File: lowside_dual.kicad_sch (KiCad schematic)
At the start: 9 parts, among them U2 2k7, U34 2k7, U35 RED, U37 RED, U38 MBR2H200SFT, U59 MBR2H200SFT, U60 NCV8403ASTT, U61 NCV8403ASTT

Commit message: update
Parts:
- renumbered U2 to R46, U34 to R47
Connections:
- net +12V renamed 12V_LED

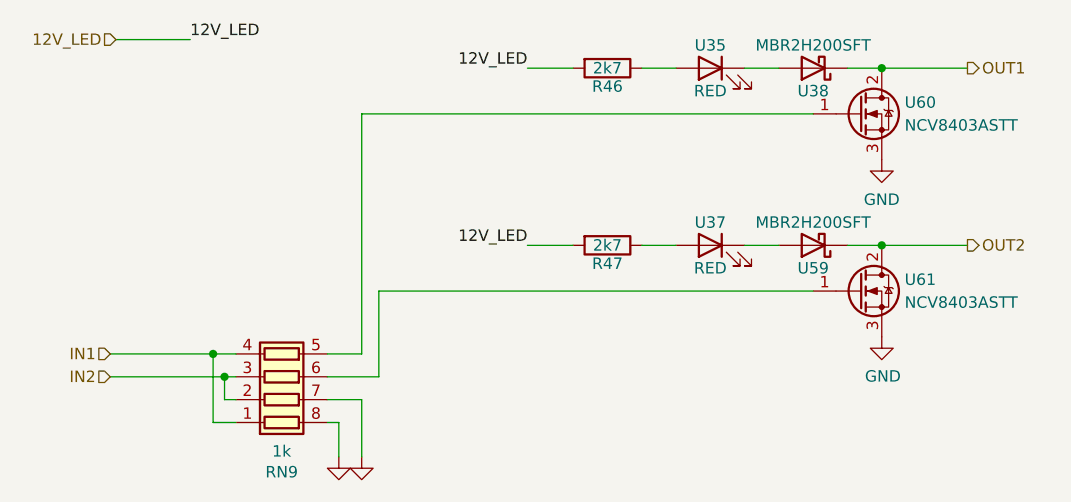
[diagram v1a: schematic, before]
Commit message: USB jack, parts and LCSC numbers, headphone jack
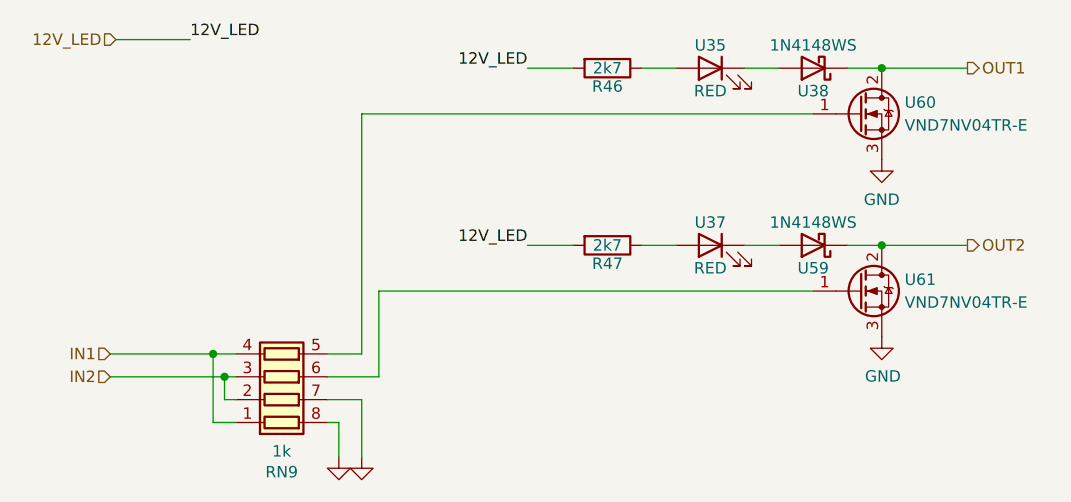
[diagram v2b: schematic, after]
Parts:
- R46, R47: footprint Resistor_SMD:R_0805_2012Metric -> Resistor_SMD:R_0402_1005Metric; LCSC (none) -> C138017
- U35, U37: footprint LED_SMD:LED_0805_2012Metric -> LED_SMD:LED_0603_1608Metric; LCSC (none) -> C84263
- U38, U59: value MBR2H200SFT -> 1N4148WS; footprint Diode_SMD:D_SOD-123 -> Diode_SMD:D_SOD-323; LCSC (none) -> C60580
- U60, U61: value NCV8403ASTT -> VND7NV04TR-E; LCSC (none) -> C155605
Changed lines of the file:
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@@
       (effects (font (size 1.27 1.27)))
     )
-    (property "Footprint" "LED_SMD:LED_0805_2012Metric" (at 161.29 62.865 0)
+    (property "Footprint" "LED_SMD:LED_0603_1608Metric" (at 161.29 62.865 0)
       (effects (font (size 1.27 1.27)) hide)
     )
@@
       (effects (font (size 1.27 1.27)))
     )
+    (property "LCSC" "C84263" (at 161.29 62.865 0)
+      (effects (font (size 1.27 1.27)) hide)
+    )
     (pin "1")
     (pin "2")
@@
       (effects (font (size 1.27 1.27)))
     )
-    (property "Footprint" "Resistor_SMD:R_0805_2012Metric" (at 149.86 61.087 90)
+    (property "Footprint" "Resistor_SMD:R_0402_1005Metric" (at 149.86 61.087 90)
       (effects (font (size 1.27 1.27)) hide)
     )
     (property "Datasheet" "" (at 149.86 62.865 0)
       (effects (font (size 1.27 1.27)))
+    )
+    (property "LCSC" "C138017" (at 149.86 62.865 90)
+      (effects (font (size 1.27 1.27)) hide)
     )
     (pin "1")
@@
       (effects (font (size 1.27 1.27)) (justify left))
     )
-    (property "Value" "NCV8403ASTT" (at 182.88 88.9 0)
+    (property "Value" "VND7NV04TR-E" (at 182.88 88.9 0)
       (effects (font (size 1.27 1.27)) (justify left))
     )
@@
       (effects (font (size 1.27 1.27)) hide)
     )
+    (property "LCSC" "C155605" (at 177.8 87.63 0)
+      (effects (font (size 1.27 1.27)) hide)
+    )
     (pin "1")
     (pin "2")
@@
       (effects (font (size 1.27 1.27)))
     )
-    (property "Footprint" "LED_SMD:LED_0805_2012Metric" (at 161.29 82.55 0)
+    (property "Footprint" "LED_SMD:LED_0603_1608Metric" (at 161.29 82.55 0)
       (effects (font (size 1.27 1.27)) hide)
     )
@@
       (effects (font (size 1.27 1.27)))
     )
+    (property "LCSC" "C84263" (at 161.29 82.55 0)
+      (effects (font (size 1.27 1.27)) hide)
+    )
     (pin "1")
     (pin "2")
@@
       (effects (font (size 1.27 1.27)))
     )
-    (property "Value" "MBR2H200SFT" (at 172.72 60.325 0)
-      (effects (font (size 1.27 1.27)))
-    )
-    (property "Footprint" "Diode_SMD:D_SOD-123" (at 172.72 62.865 0)
+    (property "Value" "1N4148WS" (at 172.72 60.325 0)
+      (effects (font (size 1.27 1.27)))
+    )
+    (property "Footprint" "Diode_SMD:D_SOD-323" (at 172.72 62.865 0)
       (effects (font (size 1.27 1.27)) hide)
     )
@@
       (effects (font (size 1.27 1.27)))
     )
+    (property "LCSC" "C60580" (at 172.72 62.865 0)
+      (effects (font (size 1.27 1.27)) hide)
+    )
     (pin "1")
     (pin "2")
@@
       (effects (font (size 1.27 1.27)))
     )
-    (property "Value" "MBR2H200SFT" (at 172.72 80.01 0)
-      (effects (font (size 1.27 1.27)))
-    )
-    (property "Footprint" "Diode_SMD:D_SOD-123" (at 172.72 82.55 0)
+    (property "Value" "1N4148WS" (at 172.72 80.01 0)
+      (effects (font (size 1.27 1.27)))
+    )
+    (property "Footprint" "Diode_SMD:D_SOD-323" (at 172.72 82.55 0)
       (effects (font (size 1.27 1.27)) hide)
     )
@@
       (effects (font (size 1.27 1.27)))
     )
+    (property "LCSC" "C60580" (at 172.72 82.55 0)
+      (effects (font (size 1.27 1.27)) hide)
+    )
     (pin "1")
     (pin "2")
@@
       (effects (font (size 1.27 1.27)))
     )
-    (property "Footprint" "Resistor_SMD:R_0805_2012Metric" (at 149.86 80.772 90)
+    (property "Footprint" "Resistor_SMD:R_0402_1005Metric" (at 149.86 80.772 90)
       (effects (font (size 1.27 1.27)) hide)
     )
     (property "Datasheet" "" (at 149.86 82.55 0)
       (effects (font (size 1.27 1.27)))
+    )
+    (property "LCSC" "C138017" (at 149.86 82.55 90)
+      (effects (font (size 1.27 1.27)) hide)
     )
     (pin "1")
@@
       (effects (font (size 1.27 1.27)) (justify left))
     )
-    (property "Value" "NCV8403ASTT" (at 182.88 69.215 0)
+    (property "Value" "VND7NV04TR-E" (at 182.88 69.215 0)
       (effects (font (size 1.27 1.27)) (justify left))
     )
@@
       (effects (font (size 1.27 1.27)) hide)
     )
+    (property "LCSC" "C155605" (at 177.8 67.945 0)
+      (effects (font (size 1.27 1.27)) hide)
+    )

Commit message: Add Stepper, fix Connector, add Testpoints, several changes
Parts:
- U35, U37: LCSC C84263 -> C2286
- U38, U59: LCSC C60580 -> C2128
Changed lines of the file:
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@@
       (effects (font (size 1.27 1.27)))
     )
-    (property "LCSC" "C84263" (at 161.29 62.865 0)
+    (property "LCSC" "C2286" (at 161.29 62.865 0)
       (effects (font (size 1.27 1.27)) hide)
     )
@@
       (effects (font (size 1.27 1.27)))
     )
-    (property "LCSC" "C84263" (at 161.29 82.55 0)
+    (property "LCSC" "C2286" (at 161.29 82.55 0)
       (effects (font (size 1.27 1.27)) hide)
     )
@@
       (effects (font (size 1.27 1.27)))
     )
-    (property "LCSC" "C60580" (at 172.72 62.865 0)
+    (property "LCSC" "C2128" (at 172.72 62.865 0)
       (effects (font (size 1.27 1.27)) hide)
     )
@@
       (effects (font (size 1.27 1.27)))
     )
-    (property "LCSC" "C60580" (at 172.72 82.55 0)
-      (effects (font (size 1.27 1.27)) hide)
-    )
+    (property "LCSC" "C2128" (at 172.72 82.55 0)
+      (effects (font (size 1.27 1.27)) hide)
+    )

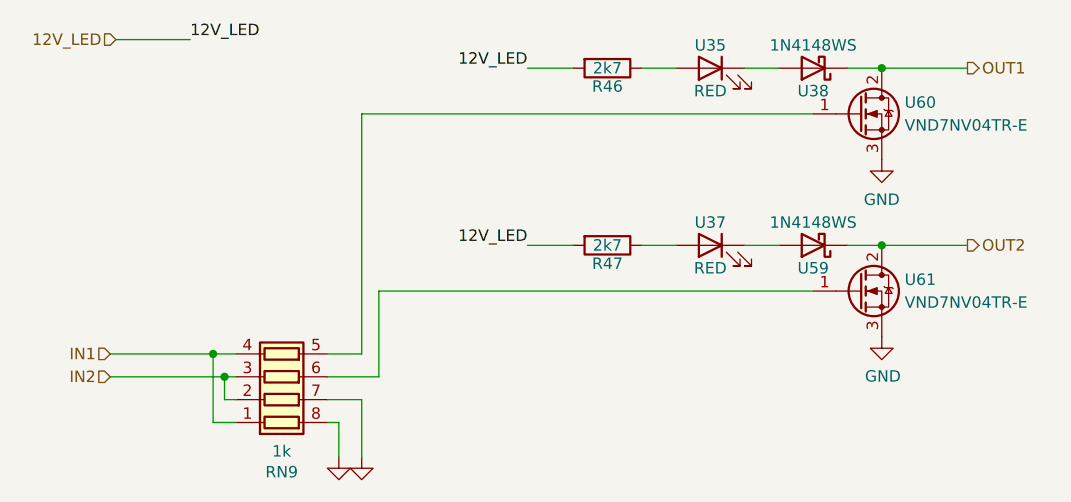
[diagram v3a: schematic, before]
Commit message: Production optimizations, voltage superv, etb sv conn
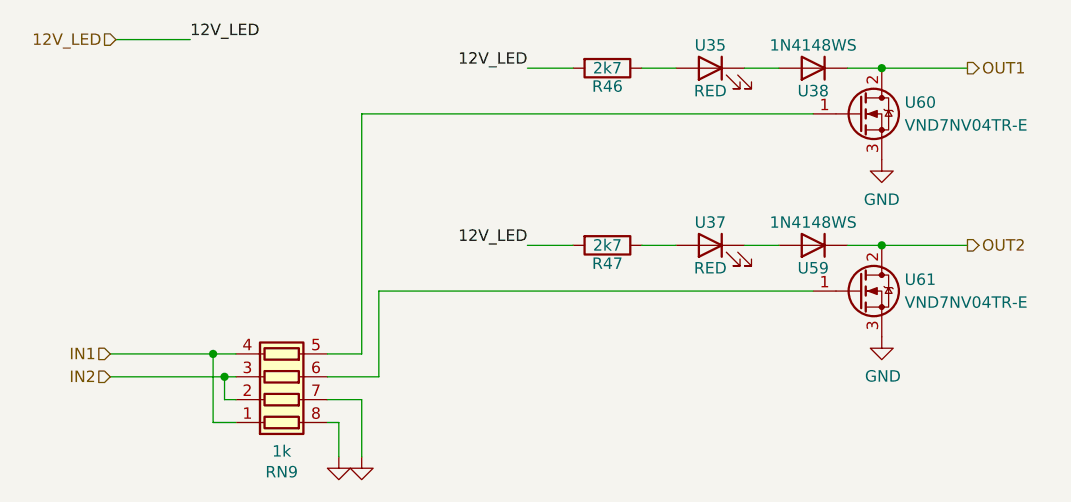
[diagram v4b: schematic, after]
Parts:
- U38, U59: symbol Device:D_Schottky -> Device:D
- U60, U61: footprint Package_TO_SOT_SMD:TO-252-2 -> Package_TO_SOT_SMD:TO-252-3_TabPin2; JLCPosOffset (none) -> 2,0; JLCRotOffset (none) -> 180; LCSC C155605 -> C262999; LCSC_alt (none) -> C155605
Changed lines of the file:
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@@
       (effects (font (size 1.27 1.27)) (justify left))
     )
-    (property "Footprint" "Package_TO_SOT_SMD:TO-252-2" (at 182.88 85.09 0)
+    (property "Footprint" "Package_TO_SOT_SMD:TO-252-3_TabPin2" (at 182.88 85.09 0)
       (effects (font (size 1.27 1.27)) hide)
     )
@@
       (effects (font (size 1.27 1.27)) hide)
     )
-    (property "LCSC" "C155605" (at 177.8 87.63 0)
+    (property "LCSC" "C262999" (at 177.8 87.63 0)
+      (effects (font (size 1.27 1.27)) hide)
+    )
+    (property "JLCPosOffset" "2,0" (at 177.8 87.63 0)
+      (effects (font (size 1.27 1.27)) hide)
+    )
+    (property "LCSC_alt" "C155605" (at 177.8 87.63 0)
+      (effects (font (size 1.27 1.27)) hide)
+    )
+    (property "JLCRotOffset" "180" (at 177.8 87.63 0)
       (effects (font (size 1.27 1.27)) hide)
     )
@@
     )
   )
-  (symbol (lib_id "Device:D_Schottky") (at 172.72 62.865 180) (unit 1)
+  (symbol (lib_id "Device:D") (at 172.72 62.865 180) (unit 1)
     (in_bom yes) (on_board yes) (dnp no)
     (property "Reference" "U38" (at 172.72 65.405 0)
@@
       (effects (font (size 1.27 1.27)) hide)
     )
-    (property "Datasheet" "" (at 172.72 62.865 0)
-      (effects (font (size 1.27 1.27)))
+    (property "Datasheet" "~" (at 172.72 62.865 0)
+      (effects (font (size 1.27 1.27)) hide)
     )
     (property "LCSC" "C2128" (at 172.72 62.865 0)
       (effects (font (size 1.27 1.27)) hide)
     )
+    (property "Sim.Device" "D" (at 172.72 62.865 0)
+      (effects (font (size 1.27 1.27)) hide)
+    )
+    (property "Sim.Pins" "1=K 2=A" (at 172.72 62.865 0)
+      (effects (font (size 1.27 1.27)) hide)
+    )
     (pin "1")
     (pin "2")
@@
     )
   )
-  (symbol (lib_id "Device:D_Schottky") (at 172.72 82.55 180) (unit 1)
+  (symbol (lib_id "Device:D") (at 172.72 82.55 180) (unit 1)
     (in_bom yes) (on_board yes) (dnp no)
     (property "Reference" "U59" (at 172.72 85.09 0)
@@
       (effects (font (size 1.27 1.27)) hide)
     )
-    (property "Datasheet" "" (at 172.72 82.55 0)
-      (effects (font (size 1.27 1.27)))
+    (property "Datasheet" "~" (at 172.72 82.55 0)
+      (effects (font (size 1.27 1.27)) hide)
     )
     (property "LCSC" "C2128" (at 172.72 82.55 0)
+      (effects (font (size 1.27 1.27)) hide)
+    )
+    (property "Sim.Device" "D" (at 172.72 82.55 0)
+      (effects (font (size 1.27 1.27)) hide)
+    )
+    (property "Sim.Pins" "1=K 2=A" (at 172.72 82.55 0)
       (effects (font (size 1.27 1.27)) hide)
     )
@@
       (effects (font (size 1.27 1.27)) (justify left))
     )
-    (property "Footprint" "Package_TO_SOT_SMD:TO-252-2" (at 182.88 65.405 0)
+    (property "Footprint" "Package_TO_SOT_SMD:TO-252-3_TabPin2" (at 182.88 65.405 0)
       (effects (font (size 1.27 1.27)) hide)
     )
@@
       (effects (font (size 1.27 1.27)) hide)
     )
-    (property "LCSC" "C155605" (at 177.8 67.945 0)
-      (effects (font (size 1.27 1.27)) hide)
-    )
+    (property "LCSC" "C262999" (at 177.8 67.945 0)
+      (effects (font (size 1.27 1.27)) hide)
+    )
+    (property "JLCPosOffset" "2,0" (at 177.8 67.945 0)
+      (effects (font (size 1.27 1.27)) hide)
+    )
+    (property "LCSC_alt" "C155605" (at 177.8 67.945 0)
+      (effects (font (size 1.27 1.27)) hide)
+    )
+    (property "JLCRotOffset" "180" (at 177.8 67.945 0)
+      (effects (font (size 1.27 1.27)) hide)
+    )
